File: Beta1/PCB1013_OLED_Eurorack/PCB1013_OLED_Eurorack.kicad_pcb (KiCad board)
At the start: 2 copper layers, 160 x 75.5 mm, 56 parts, among them J1 Axoloti_40Pin, J2 FPC_20POS, U1 MCP3008T-I/SL, U10 OLED_128x32_I2C, U2 MCP3008T-I/SL, U20 OLED_128x32_I2C, U3 I2C_1x4MUX_TCA9546A, U30 OLED_128x32_I2C, U40 OLED_128x32_I2C

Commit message: Rough placement
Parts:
- removed CS_0_7, GND0, SPI_CLK_0, SPI_MISO_0, SPI_MOSI_0, VCC0: CONN_01X01, Liberry:single_0.1
- removed JOY0, JOY1, JOY2, JOY3: XYJOY_Alps, Liberry:JOY_ALPS_RKJXV1224005
- removed R0, R1, R2, R3, R4, R5, R6, R7: POT, Liberry:POT_ALPS_RK09K1130BM4
- removed U1, U2: MCP3008T-I/SL, Liberry:SOIC-16
- added C4: 0.1u, Capacitor_SMD:C_0603_1608Metric, F.Cu at (-87.4, -144.0)
- added RC1: 10K, Resistor_SMD:R_0603_1608Metric, F.Cu at (-87.4, -142.5)
- added RC50: 10K, Resistor_SMD:R_0603_1608Metric, F.Cu at (-84.4, -144.0)
- added RC60: 10K, Resistor_SMD:R_0603_1608Metric, F.Cu at (-87.4, -141.0)
- added RC70: 10K, Resistor_SMD:R_0603_1608Metric, F.Cu at (-84.4, -142.5)
- added RC80: 10K, Resistor_SMD:R_0603_1608Metric, F.Cu at (-81.4, -144.0)
- added RD1: 10K, Resistor_SMD:R_0603_1608Metric, F.Cu at (-87.4, -139.5)
- added RD50: 10K, Resistor_SMD:R_0603_1608Metric, F.Cu at (-84.4, -141.0)
- added RD60: 10K, Resistor_SMD:R_0603_1608Metric, F.Cu at (-81.4, -142.5)
- added RD70: 10K, Resistor_SMD:R_0603_1608Metric, F.Cu at (-84.4, -139.5)
- added RD80: 10K, Resistor_SMD:R_0603_1608Metric, F.Cu at (-81.4, -141.0)
- added RR1: 10K, Resistor_SMD:R_0603_1608Metric, F.Cu at (-81.4, -139.5)
- added U4: I2C_1x4MUX_TCA9546A, Liberry:SOIC-16_1.27x5.4, F.Cu at (-110.5, -171.4)
- added U50: OLED_128x32_I2C, Liberry:OLED_128x32, F.Cu at (10.2, -61.0)
- added U5000: STM32F103C8T6_BLUE_PILL, Liberry:BLUEPILL_CORTEXM3_STM32F103C8T6_THIN, F.Cu at (76.2, -73.7)
- added U60: OLED_128x32_I2C, Liberry:OLED_128x32, F.Cu at (10.2, -47.0)
- added U70: OLED_128x32_I2C, Liberry:OLED_128x32, F.Cu at (10.2, -33.0)
- added U80: OLED_128x32_I2C, Liberry:OLED_128x32, F.Cu at (10.2, -19.1)
- moved RC10 433.7 mm to (432.4, 21.6)
- moved RC20 433.7 mm to (471.8, 21.6)
- moved RD10 433.7 mm to (432.4, 19.1)
- moved RD20 433.7 mm to (471.8, 19.1)
- moved REF** 244.2 mm to (-87.6, -29.2)
- moved REF** 243.9 mm to (-85.1, -19.1)
- moved U3 243.2 mm to (-143.5, -168.9)
- moved C3 192.5 mm to (249.2, -103.9)
- moved RC0 192.5 mm to (246.6, -100.8)
- moved RD0 192.5 mm to (246.6, -103.9)
- moved RR0 192.5 mm to (249.2, -100.8)
- moved J2 176.2 mm to (-53.3, -76.2), turned to 180 degrees
- moved RC30 167.9 mm to (219.1, -156.2)
- moved RD30 167.9 mm to (219.1, -158.8)
- moved REF** 151.8 mm to (7.50, -3.00)
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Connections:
- J1 pad 4: /I2C_SCL -> /I2C_SCL_AXO
- J1 pad 5: /I2C_SDA -> /I2C_SDA_AXO
- J1 pad 8: /!OLED_RESET -> /RESET_AXO
- J2 pad 17: /!OLED_RESET -> /RESET_AXO
- J2 pad 3: /I2C_SCL -> /I2C_SC_AXO
- J2 pad 4: /I2C_SDA -> /I2C_SDA_AXO
- J2 pad 8: /RX -> /RX_AXO
- J2 pad 9: /TX -> /TX_AXO
- RC0 pad 2: /I2C_SCL -> /I2C_SCL_EXT
- RD0 pad 2: /I2C_SDA -> /I2C_SDA_EXT
- U3 pad 14: /I2C_SCL -> /I2C_SCL_EXT
- U3 pad 15: /I2C_SDA -> /I2C_SDA_EXT
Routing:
- net +3V3: track 647.5 -> 0.00 mm, vias 12 -> 0
- net /!OLED_RESET: track 159.9 -> 0.00 mm, vias 7 -> 0
- net /JOY_0_SW: track 146.7 -> 0.00 mm, vias 4 -> 0
- net /CS_0_7: track 146.2 -> 0.00 mm, vias 1 -> 0
- net /I2C_SDA: track 130.6 -> 0.00 mm, vias 2 -> 0
- net /JOY_0_0: track 126.6 -> 0.00 mm, vias 2 -> 0
- net /I2C_SCL: track 126.4 -> 0.00 mm, vias 1 -> 0
- net /JOY_0_1: track 112.9 -> 0.00 mm, vias 2 -> 0
- net /JOY_2_SW: track 112.3 -> 0.00 mm, vias 2 -> 0
- net /CS_8_15: track 107.1 -> 0.00 mm, vias 4 -> 0
- net GND: track 105.7 -> 0.00 mm, vias 5 -> 0
- net /JOY_3_SW: track 105.0 -> 0.00 mm
- net /JOY_1_SW: track 95.9 -> 0.00 mm, vias 2 -> 0
- net /SPI_MOSI: track 90.9 -> 0.00 mm, vias 4 -> 0
- net /JOY_1_0: track 90.3 -> 0.00 mm, vias 2 -> 0
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- removed copper zone on B.Cu, net GND
- removed copper zone on F.Cu, net GND
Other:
- board size 160 x 75.5 mm -> 55.6 x 128.5 mm
- board text removed: "MCP3008T-I/SL"
- board text removed: "RKJXV1224005"

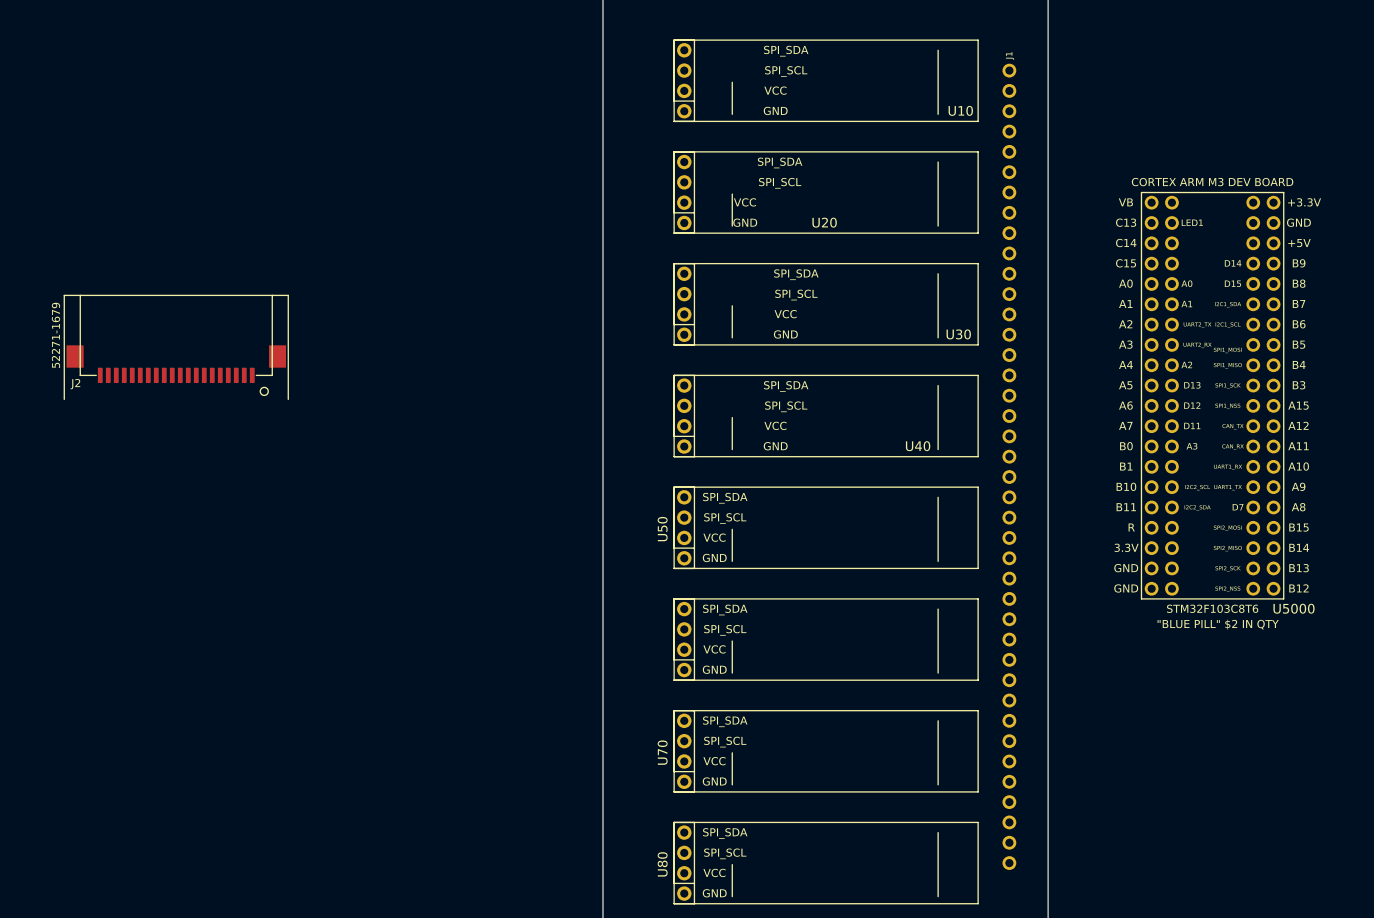
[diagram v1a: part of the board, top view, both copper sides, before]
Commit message: Removed 40 pin header
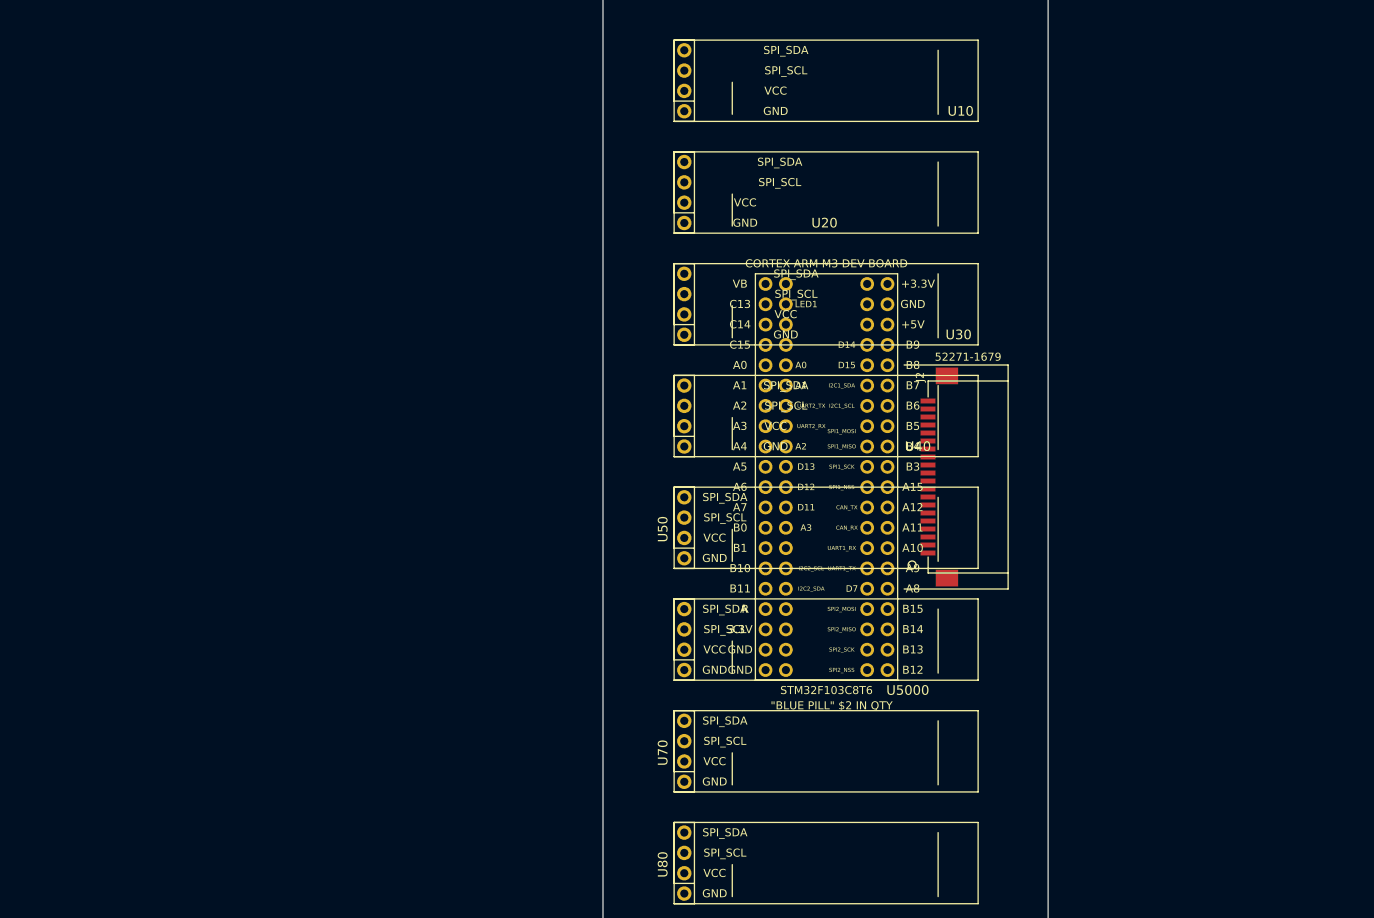
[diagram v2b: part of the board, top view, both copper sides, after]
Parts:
- removed J1: Axoloti_40Pin, Liberry:Axoloti-40x1_slim
- moved J2 94.8 mm to (40.6, -63.5), turned to 90 degrees
- moved U5000 49.3 mm to (27.9, -63.5)
